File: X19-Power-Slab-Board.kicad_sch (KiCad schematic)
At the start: 33 parts, among them J2 796636-6, J3 Conn_01x02_Pin, J4 Conn_01x04_Pin, J5 Conn_01x04_Pin, Q1 TSM340N06CP_ROG, U2 MIC5504-3.3YM5-TR, U3 INA237AIDGSR, U4 TMP1075NDRLR, U6 TCAN1044AVDRQ1

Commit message: fixed power labeling
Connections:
- net GND: now also U4.4 (A0)
- net SCL: now also U3.5 (SCL), U4.1 (SCL)
- net SDA: now also U3.4 (SDA), U4.6 (SDA)
- net 12V renamed +12V
- net 3.3V renamed +3.3V
- net 48V renamed +48V
- net 5.2V renamed +5.2V
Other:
- moved on the sheet: R10, R9, TP3, TP5

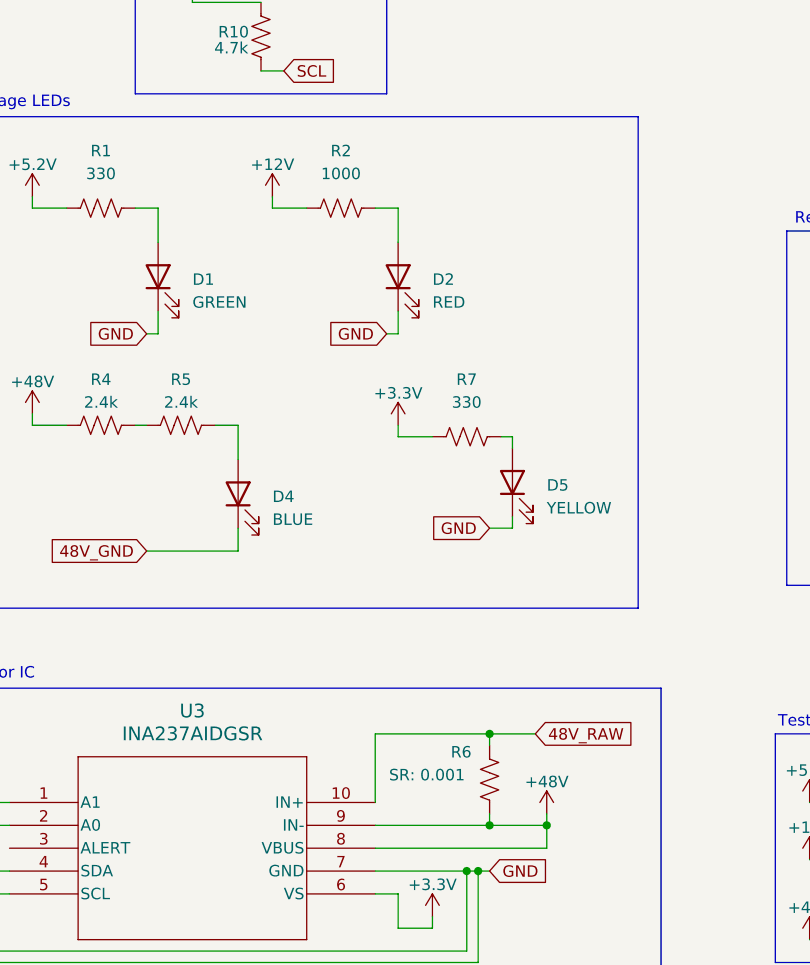
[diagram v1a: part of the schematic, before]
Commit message: add footprints for standardized components
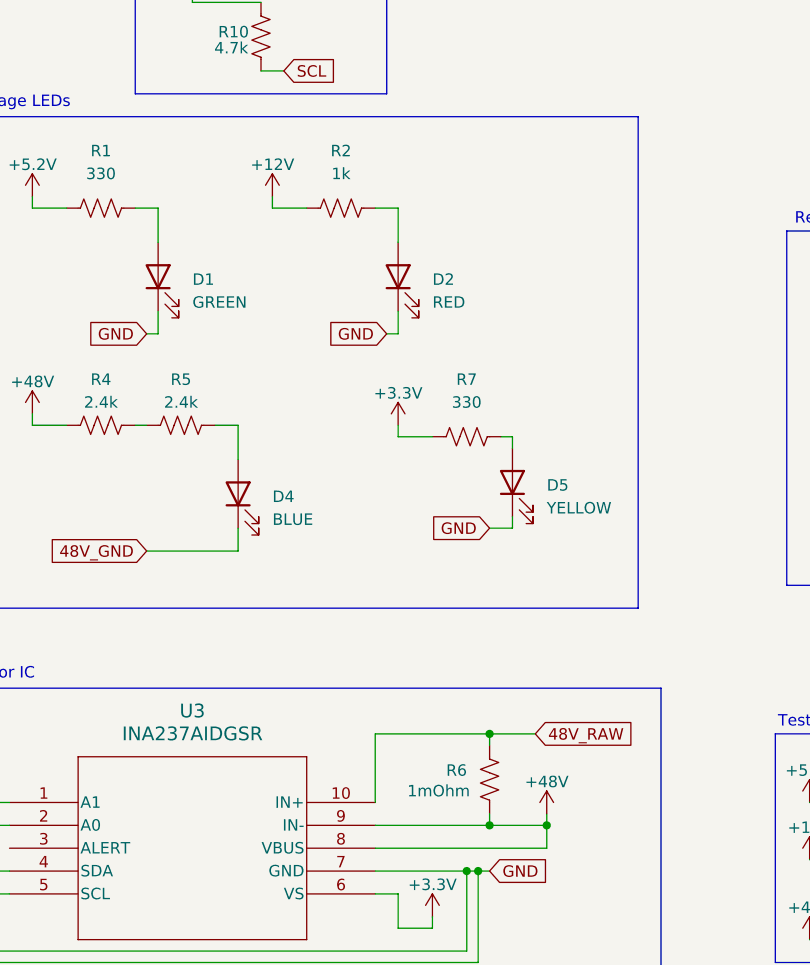
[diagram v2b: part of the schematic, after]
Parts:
- C1, C2, C3: footprint (none) -> Capacitor_THT:CP_Radial_D22.0mm_P10.00mm_SnapIn; Manufacturer_Part_Number (none) -> UVZ2A331MHD1TO
- C4: footprint (none) -> Capacitor_SMD:C_0603_1608Metric
- C5: footprint SOT-23-5_MC_MCH -> Capacitor_SMD:C_0603_1608Metric
- D1, D2, D4, D5: footprint (none) -> LED_SMD:LED_0603_1608Metric
- D6: footprint SMB_STM -> Diode_SMD:D_SOD-323
- J2: footprint CON6_P5MM_VER_TERM-BLK_TYC -> (none)
- J3, J4, J5: now left out of the parts list
- Q1: footprint Package_DFN_QFN:Nordic_AQFN-94-1EP_7x7mm_P0.4mm -> Package_TO_SOT_SMD:TO-252-2
- R1, R10, R4, R5, R7, R8, R9: footprint (none) -> Resistor_SMD:R_0603_1608Metric
- R2: value 1000 -> 1k; footprint (none) -> Resistor_SMD:R_0603_1608Metric
- R6: value SR: 0.001 -> 1mOhm; footprint (none) -> Resistor_SMD:R_1206_3216Metric; Manufacturer_Part_Number (none) -> CSNL1206FT1L00
- TP1, TP2, TP3, TP4, TP5: footprint Package_SO:SOIC-24W_7.5x15.4mm_P1.27mm -> (none); now left out of the parts list
- U2: footprint SOT-23-5_MC_MCH -> Package_TO_SOT_SMD:SOT-23-5
- U3: footprint VSSOP_IDGSR_TEX -> Package_SO:TSSOP-10_3x3mm_P0.5mm
- U4: footprint SOT5X3-6_DRL_TEX -> Package_TO_SOT_SMD:SOT-563
- U6: footprint D0008A-IPC_A -> Package_SO:SOIC-8_3.9x4.9mm_P1.27mm
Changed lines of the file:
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@@
 		(body_style 1)
 		(exclude_from_sim no)
-		(in_bom yes)
+		(in_bom no)
 		(on_board yes)
 		(in_pos_files yes)
@@
 			)
 		)
-		(property "Footprint" "CON6_P5MM_VER_TERM-BLK_TYC"
+		(property "Footprint" ""
 			(at 138.43 80.01 0)
 			(hide yes)
@@
 			)
 		)
-		(property "Footprint" "SOT-23-5_MC_MCH"
+		(property "Footprint" "Package_TO_SOT_SMD:SOT-23-5"
 			(at 203.2 87.63 0)
 			(hide yes)
@@
 		(body_style 1)
 		(exclude_from_sim no)
-		(in_bom yes)
+		(in_bom no)
 		(on_board yes)
 		(in_pos_files yes)
@@
 			)
 		)
-		(property "Footprint" "Package_SO:SOIC-24W_7.5x15.4mm_P1.27mm"
+		(property "Footprint" ""
 			(at 161.29 173.99 0)
 			(hide yes)
@@
 			)
 		)
-		(property "Value" "1000"
+		(property "Value" "1k"
 			(at 64.77 104.14 90)
 			(show_name no)
@@
 			)
 		)
-		(property "Footprint" ""
+		(property "Footprint" "Resistor_SMD:R_0603_1608Metric"
 			(at 65.024 106.934 90)
 			(hide yes)
@@
 			)
 		)
-		(property "Footprint" "VSSOP_IDGSR_TEX"
+		(property "Footprint" "Package_SO:TSSOP-10_3x3mm_P0.5mm"
 			(at 27.94 173.99 0)
 			(hide yes)
@@
 		(body_style 1)
 		(exclude_from_sim no)
-		(in_bom yes)
+		(in_bom no)
 		(on_board yes)
 		(in_pos_files yes)
@@
 			)
 		)
-		(property "Footprint" "Package_SO:SOIC-24W_7.5x15.4mm_P1.27mm"
+		(property "Footprint" ""
 			(at 161.29 185.42 0)
 			(hide yes)
@@
 			)
 		)
-		(property "Footprint" ""
+		(property "Footprint" "Resistor_SMD:R_0603_1608Metric"
 			(at 38.354 106.934 90)
 			(hide yes)
@@
 			)
 		)
-		(property "Footprint" "SOT-23-5_MC_MCH"
+		(property "Footprint" "Capacitor_SMD:C_0603_1608Metric"
 			(at 252.4252 95.25 0)
 			(hide yes)
@@
 			)
 		)
-		(property "Footprint" ""
+		(property "Footprint" "Resistor_SMD:R_0603_1608Metric"
 			(at 129.286 121.666 90)
 			(hide yes)
@@
 			)
 		)
-		(property "Footprint" "SMB_STM"
+		(property "Footprint" "Diode_SMD:D_SOD-323"
 			(at 133.35 125.73 0)
 			(hide yes)
@@
 			)
 		)
-		(property "Footprint" ""
+		(property "Footprint" "LED_SMD:LED_0603_1608Metric"
 			(at 83.82 138.43 0)
 			(hide yes)
@@
 			)
 		)
-		(property "Footprint" ""
+		(property "Footprint" "Capacitor_THT:CP_Radial_D22.0mm_P10.00mm_SnapIn"
 			(at 66.04 38.1 0)
 			(hide yes)
@@
 			)
 		)
+		(property "Manufacturer_Part_Number" "UVZ2A331MHD1TO"
+			(at 66.04 38.1 0)
+			(hide yes)
+			(show_name no)
+			(do_not_autoplace no)
+			(effects
+				(font
+					(size 1.27 1.27)
+				)
+			)
+		)
 		(pin "2"
 		)
@@
 			)
 		)
-		(property "Footprint" ""
+		(property "Footprint" "Resistor_SMD:R_0603_1608Metric"
 			(at 78.994 132.334 90)
 			(hide yes)
@@
 		(dnp no)
 		(property "Reference" "R6"
-			(at 76.962 168.402 0)
+			(at 76.454 170.434 0)
 			(show_name no)
 			(do_not_autoplace no)
@@
 			)
 		)
-		(property "Value" "SR: 0.001"
-			(at 70.104 170.942 0)
+		(property "Value" "1mOhm"
+			(at 72.136 172.72 0)
 			(show_name no)
 			(do_not_autoplace no)
@@
 			)
 		)
-		(property "Footprint" ""
+		(property "Footprint" "Resistor_SMD:R_1206_3216Metric"
 			(at 82.296 171.704 90)
 			(hide yes)
@@
 			)
 		)
+		(property "Manufacturer_Part_Number" "CSNL1206FT1L00"
+			(at 81.28 171.45 0)
+			(hide yes)
+			(show_name no)
+			(do_not_autoplace no)
+			(effects
+				(font
+					(size 1.27 1.27)
+				)
+			)
+		)
 		(pin "1"
 		)
@@
 		(body_style 1)
 		(exclude_from_sim no)
-		(in_bom yes)
+		(in_bom no)
 		(on_board yes)
 		(in_pos_files yes)
@@
 		(body_style 1)
 		(exclude_from_sim no)
-		(in_bom yes)
+		(in_bom no)
 		(on_board yes)
 		(in_pos_files yes)
@@
 			)
 		)
-		(property "Footprint" "Package_SO:SOIC-24W_7.5x15.4mm_P1.27mm"
+		(property "Footprint" ""
 			(at 130.81 173.99 0)
 			(hide yes)
@@
 			)
 		)
-		(property "Footprint" ""
+		(property "Footprint" "Capacitor_THT:CP_Radial_D22.0mm_P10.00mm_SnapIn"
 			(at 38.1 38.1 0)
 			(hide yes)
@@
 			)
 		)
+		(property "Manufacturer_Part_Number" "UVZ2A331MHD1TO"
+			(at 38.1 38.1 0)
+			(hide yes)
+			(show_name no)
+			(do_not_autoplace no)
+			(effects
+				(font
+					(size 1.27 1.27)
+				)
+			)
+		)
 		(pin "2"
 		)
@@
 			)
 		)
-		(property "Footprint" ""
+		(property "Footprint" "Resistor_SMD:R_0603_1608Metric"
 			(at 38.354 131.064 90)
 			(hide yes)
@@
 			)
 		)
-		(property "Footprint" ""
+		(property "Footprint" "Resistor_SMD:R_0603_1608Metric"
 			(at 54.864 88.646 90)
 			(hide yes)
@@
 			)
 		)
-		(property "Footprint" ""
+		(property "Footprint" "LED_SMD:LED_0603_1608Metric"
 			(at 71.12 115.57 0)
 			(hide yes)
@@
 		(body_style 1)
 		(exclude_from_sim no)
-		(in_bom yes)
+		(in_bom no)
 		(on_board yes)
 		(in_pos_files yes)
@@
 			)
 		)
-		(property "Footprint" "Package_SO:SOIC-24W_7.5x15.4mm_P1.27mm"
+		(property "Footprint" ""
 			(at 130.81 189.23 0)
 			(hide yes)
@@
 			)
 		)
-		(property "Footprint" ""
+		(property "Footprint" "LED_SMD:LED_0603_1608Metric"
 			(at 53.34 139.7 0)
 			(hide yes)
@@
 			)
 		)
-		(property "Footprint" ""
+		(property "Footprint" "Resistor_SMD:R_0603_1608Metric"
 			(at 54.864 74.676 90)
 			(hide yes)
@@
 			)
 		)
-		(property "Footprint" "SOT5X3-6_DRL_TEX"
+		(property "Footprint" "Package_TO_SOT_SMD:SOT-563"
 			(at 209.55 38.1 0)
 			(hide yes)
@@
 			)
 		)
-		(property "Footprint" ""
+		(property "Footprint" "Capacitor_THT:CP_Radial_D22.0mm_P10.00mm_SnapIn"
 			(at 52.07 38.1 0)
 			(hide yes)
@@
 			)
 		)
+		(property "Manufacturer_Part_Number" "UVZ2A331MHD1TO"
+			(at 52.07 38.1 0)
+			(hide yes)
+			(show_name no)
+			(do_not_autoplace no)
+			(effects
+				(font
+					(size 1.27 1.27)
+				)
+			)
+		)
 		(pin "2"
 		)
@@
 			)
 		)
-		(property "Footprint" "D0008A-IPC_A"
+		(property "Footprint" "Package_SO:SOIC-8_3.9x4.9mm_P1.27mm"
 			(at 123.19 34.29 0)
 			(hide yes)
@@
 			)
 		)
-		(property "Footprint" ""
+		(property "Footprint" "LED_SMD:LED_0603_1608Metric"
 			(at 44.45 115.57 0)
 			(hide yes)
@@
 			)
 		)
-		(property "Footprint" ""
+		(property "Footprint" "Capacitor_SMD:C_0603_1608Metric"
 			(at 80.9752 41.91 0)
 			(hide yes)
@@
 			)
 		)
-		(property "Footprint" "Package_DFN_QFN:Nordic_AQFN-94-1EP_7x7mm_P0.4mm"
+		(property "Footprint" "Package_TO_SOT_SMD:TO-252-2"
 			(at 137.16 140.97 0)
 			(hide yes)
@@
 		(body_style 1)
 		(exclude_from_sim no)
-		(in_bom yes)
+		(in_bom no)
 		(on_board yes)
 		(in_pos_files yes)
@@
 			)
 		)
-		(property "Footprint" "Package_SO:SOIC-24W_7.5x15.4mm_P1.27mm"
+		(property "Footprint" ""
 			(at 130.81 180.34 0)
 			(hide yes)
@@
 		(body_style 1)
 		(exclude_from_sim no)
-		(in_bom yes)
+		(in_bom no)
 		(on_board yes)
 		(in_pos_files yes)
@@
 			)
 		)
-		(property "Footprint" ""
+		(property "Footprint" "Resistor_SMD:R_0603_1608Metric"
 			(at 47.244 131.064 90)
 			(hide yes)
